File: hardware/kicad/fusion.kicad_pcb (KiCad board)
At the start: 2 copper layers, 33 x 59.9 mm, 36 parts, among them J1 BATTERY, J2 LSM6DSOX, J3 PICKIT, J4 HC-05, J5 FLEX, J7 FTDI, SW1 BUTTON, SW2 POWER, SW3 UART, U1 MCP1603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

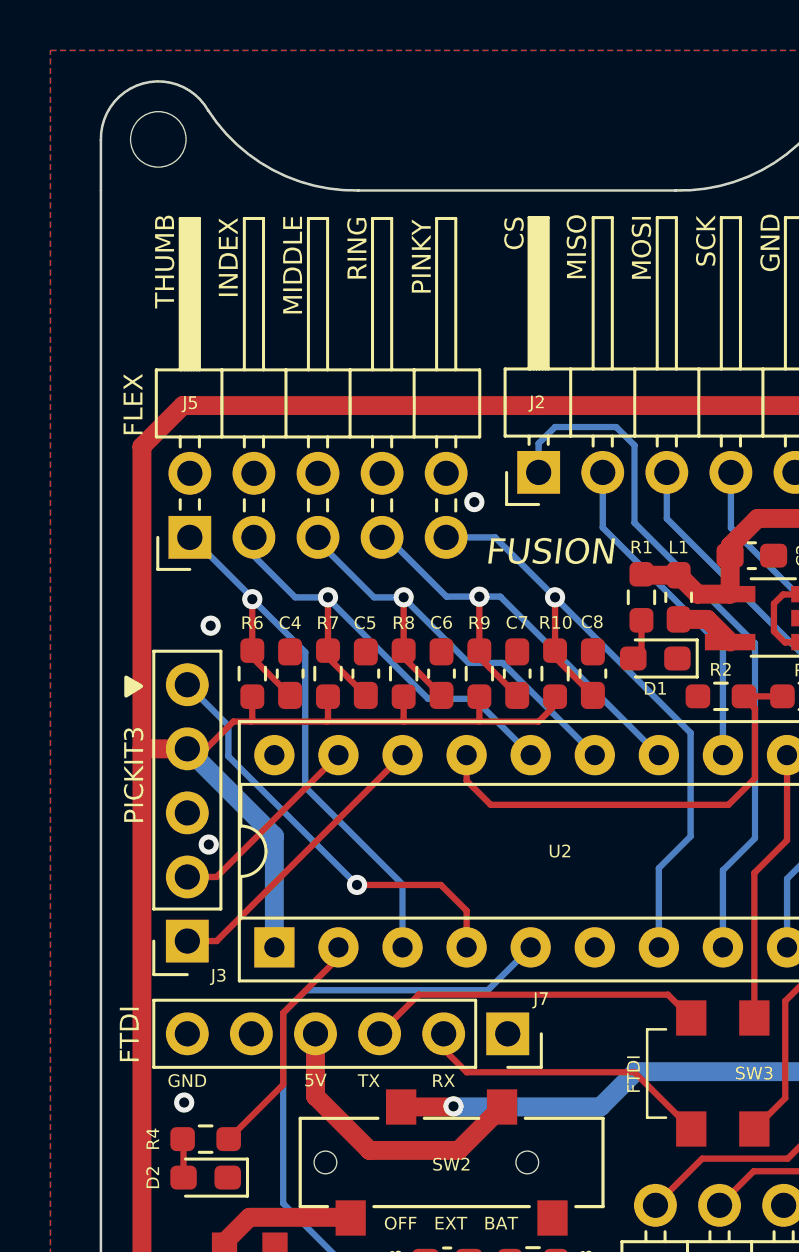
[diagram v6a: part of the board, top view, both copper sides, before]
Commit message: Rename FTDI to USB
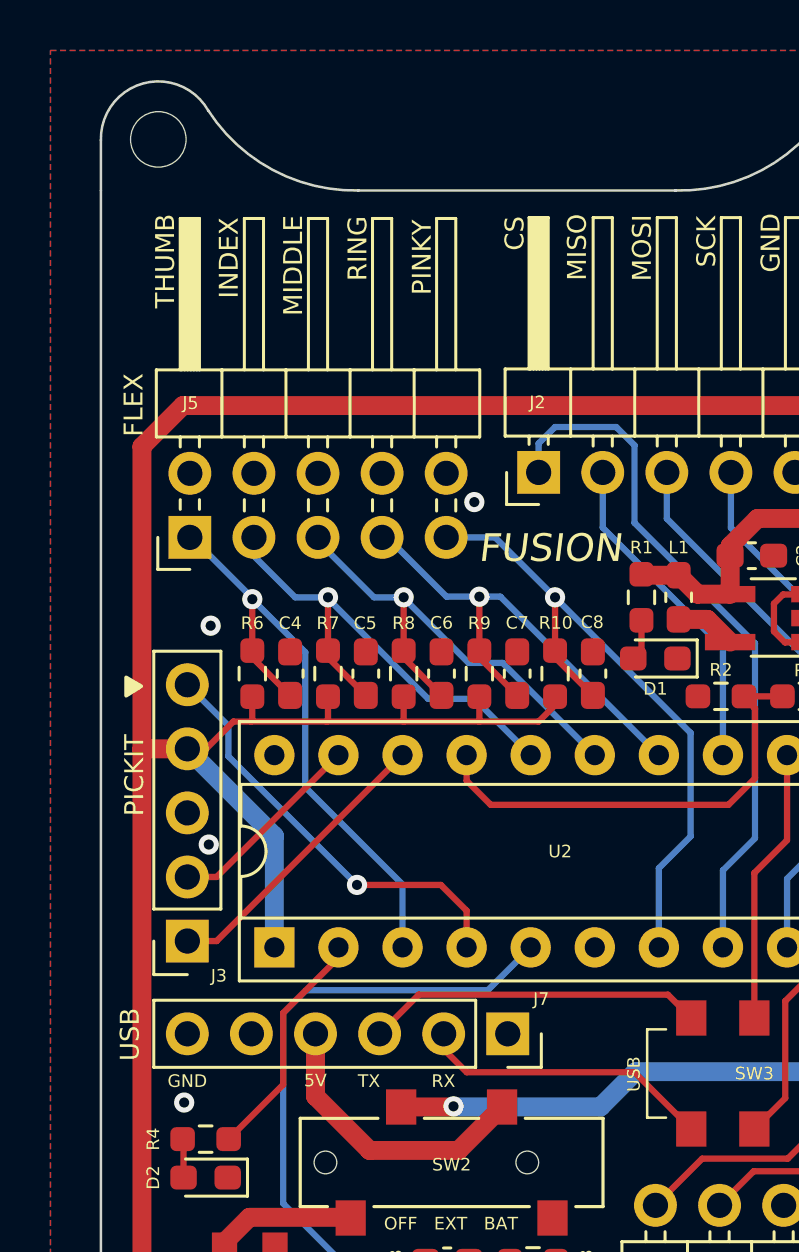
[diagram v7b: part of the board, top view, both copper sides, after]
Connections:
- net FTDI_5V renamed USB_5V
- net FTDI_RX renamed USB_RX
- net FTDI_TX renamed USB_TX
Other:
- board text added: "PICKIT"
- board text added: "USB"
- board text removed: "FTDI"
- board text removed: "PICKIT3"
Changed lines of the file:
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@@
   (net 16 "THUMB")
   (net 17 "unconnected-(J7-Pad1)")
-  (net 18 "FTDI_RX")
-  (net 19 "FTDI_TX")
-  (net 20 "FTDI_5V")
+  (net 18 "USB_RX")
+  (net 19 "USB_TX")
+  (net 20 "USB_5V")
   (net 21 "unconnected-(J7-Pad5)")
   (net 22 "Net-(D1-Pad2)")
@@
       (net 17 "unconnected-(J7-Pad1)") (pinfunction "Pin_1") (pintype "passive+no_connect"))
     (pad "2" thru_hole oval (at 0 2.54 270) (size 1.7 1.7) (drill 1) (layers *.Cu *.Mask)
-      (net 18 "FTDI_RX") (pinfunction "Pin_2") (pintype "passive"))
+      (net 18 "USB_RX") (pinfunction "Pin_2") (pintype "passive"))
     (pad "3" thru_hole oval (at 0 5.08 270) (size 1.7 1.7) (drill 1) (layers *.Cu *.Mask)
-      (net 19 "FTDI_TX") (pinfunction "Pin_3") (pintype "passive"))
+      (net 19 "USB_TX") (pinfunction "Pin_3") (pintype "passive"))
     (pad "4" thru_hole oval (at 0 7.62 270) (size 1.7 1.7) (drill 1) (layers *.Cu *.Mask)
-      (net 20 "FTDI_5V") (pinfunction "Pin_4") (pintype "passive"))
+      (net 20 "USB_5V") (pinfunction "Pin_4") (pintype "passive"))
     (pad "5" thru_hole oval (at 0 10.16 270) (size 1.7 1.7) (drill 1) (layers *.Cu *.Mask)
       (net 21 "unconnected-(J7-Pad5)") (pinfunction "Pin_5") (pintype "passive+no_connect"))
@@
       (net 23 "BUTTON") (pinfunction "RC5/CCP1/P1A") (pintype "bidirectional"))
     (pad "6" thru_hole oval (at 0 12.7 90) (size 1.6 1.6) (drill 0.8) (layers *.Cu *.Mask)
-      (net 33 "unconnected-(U2-Pad6)") (pinfunction "RC4/C2OUT/P1B") (pintype "bidirectional"))
+      (net 33 "unconnected-(U2-Pad6)") (pinfunction "RC4/C2OUT/P1B") (pintype "bidirectional+no_connect"))
     (pad "7" thru_hole oval (at 0 15.24 90) (size 1.6 1.6) (drill 0.8) (layers *.Cu *.Mask)
       (net 12 "PINKY") (pinfunction "RC3/AN7/C12IN3-/P1C") (pintype "bidirectional"))
@@
       (net 24 "RX") (pinfunction "B") (pintype "passive"))
     (pad "3" smd rect (at 2.5 2.2 180) (size 1.2 1.4) (layers "F.Cu" "F.Paste" "F.Mask")
-      (net 19 "FTDI_TX") (pinfunction "C") (pintype "passive"))
+      (net 19 "USB_TX") (pinfunction "C") (pintype "passive"))
     (pad "4" smd rect (at -2.5 -2.2 180) (size 1.2 1.4) (layers "F.Cu" "F.Paste" "F.Mask")
       (net 11 "BT_RX") (pinfunction "A") (pintype "passive"))
@@
       (net 25 "TX") (pinfunction "B") (pintype "passive"))
     (pad "6" smd rect (at 2.5 -2.2 180) (size 1.2 1.4) (layers "F.Cu" "F.Paste" "F.Mask")
-      (net 18 "FTDI_RX") (pinfunction "C") (pintype "passive"))
+      (net 18 "USB_RX") (pinfunction "C") (pintype "passive"))
     (model "${KIPRJMOD}/models/SPDT.step"
       (offset (xyz 0 0 3.5))
@@
       (net 31 "unconnected-(SW2-Pad1)") (pinfunction "1") (pintype "passive+no_connect"))
     (pad "2" smd rect (at -2 2.2 180) (size 1.2 1.4) (layers "F.Cu" "F.Paste" "F.Mask")
-      (net 20 "FTDI_5V") (pinfunction "2") (pintype "passive"))
+      (net 20 "USB_5V") (pinfunction "2") (pintype "passive"))
     (pad "3" smd rect (at 2 2.2 180) (size 1.2 1.4) (layers "F.Cu" "F.Paste" "F.Mask")
       (net 26 "Net-(C1-Pad1)") (pinfunction "3") (pintype "passive"))
@@
   (gr_arc (start 165.775 64.825) (mid 163.190649 67.197979) (end 159.775 68) (layer "Edge.Cuts") (width 0.1))
   (gr_arc (start 159.824452 119.3) (mid 163.212162 120.114076) (end 165.774452 122.475) (layer "Edge.Cuts") (width 0.1))
-  (gr_arc (start 137 66) (mid 138.667917 63.758017) (end 141.250548 64.825) (layer "Edge.Cuts") (width 0.1))
+  (gr_arc (start 137 66) (mid 138.667917 63.758018) (end 141.250548 64.825) (layer "Edge.Cuts") (width 0.1))
   (gr_arc (start 165.775 64.825) (mid 168.357369 63.758186) (end 170.025 66) (layer "Edge.Cuts") (width 0.1))
   (gr_line (start 137 119.3) (end 137 68) (layer "Edge.Cuts") (width 0.1))
@@
     (effects (font (size 0.5 0.5) (thickness 0.1)))
   )
-  (gr_text "FUSION" (at 154.8 82.325) (layer "F.SilkS")
-    (effects (font (size 1 1) (thickness 0.25) italic))
+  (gr_text "FUSION" (at 154.8 82.175) (layer "F.SilkS")
+    (effects (font (size 1.1 1.1) (thickness 0.275) italic))
   )
   (gr_text "TX" (at 160.525 117.75 90) (layer "F.SilkS")
@@
     (effects (font (size 0.75 0.75) (thickness 0.125)))
   )
-  (gr_text "FTDI" (at 158.125 103.025 90) (layer "F.SilkS")
+  (gr_text "USB" (at 158.125 103.025 90) (layer "F.SilkS")
     (effects (font (size 0.5 0.5) (thickness 0.1)))
   )
-  (gr_text "PICKIT3" (at 138.325 91.175 90) (layer "F.SilkS")
+  (gr_text "PICKIT" (at 138.325 91.175 90) (layer "F.SilkS")
     (effects (font (size 0.75 0.75) (thickness 0.125)))
   )
@@
     (effects (font (size 0.75 0.75) (thickness 0.125)))
   )
-  (gr_text "FTDI" (at 138.15 101.45 90) (layer "F.SilkS")
-    (effects (font (size 0.75 0.75) (thickness 0.125)))
-  )
+  (gr_text "USB" (at 138.15 101.45 90) (layer "F.SilkS")
+    (effects (font (size 0.75 0.75) (thickness 0.125)))
+  )

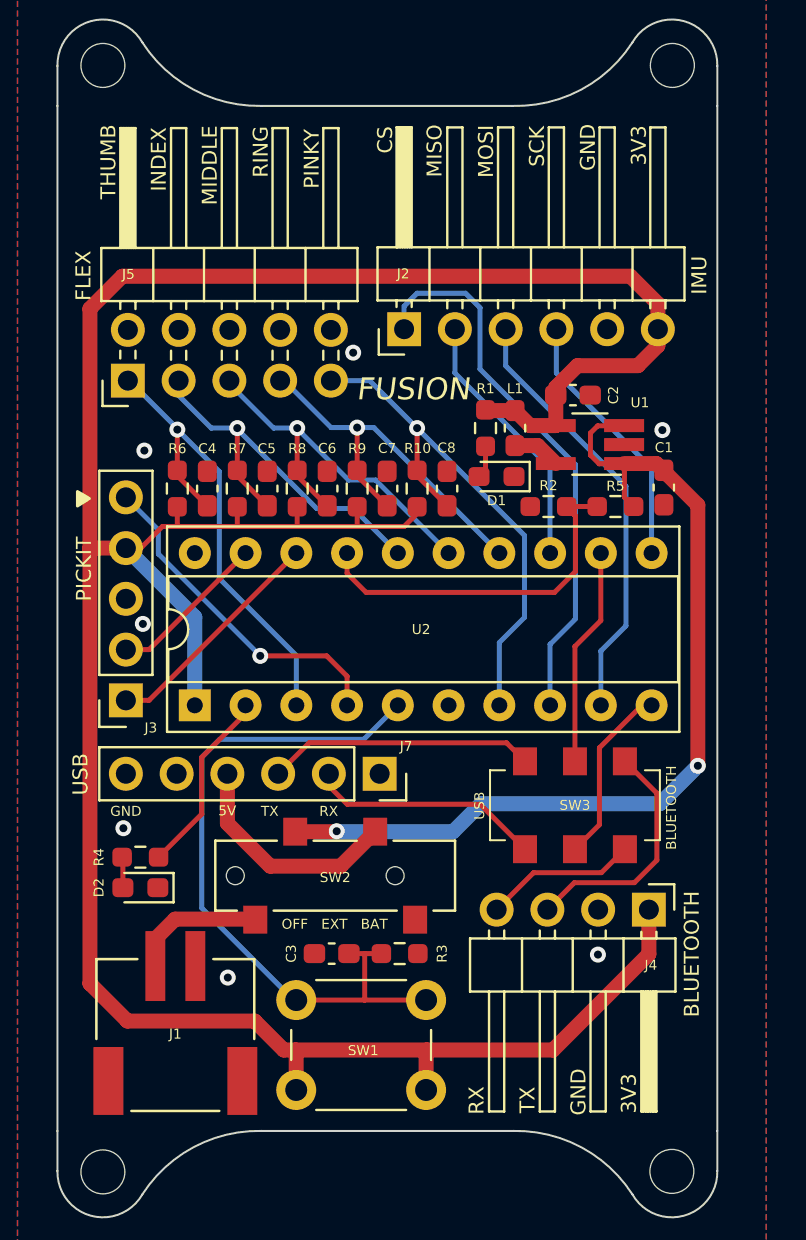
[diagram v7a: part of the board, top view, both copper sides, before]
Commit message: Power HC-05 from raw power source
BT module has an LDO that requires at least 3V6.
Powering from 3V3 causes improper regulation and
browns out the entire system.
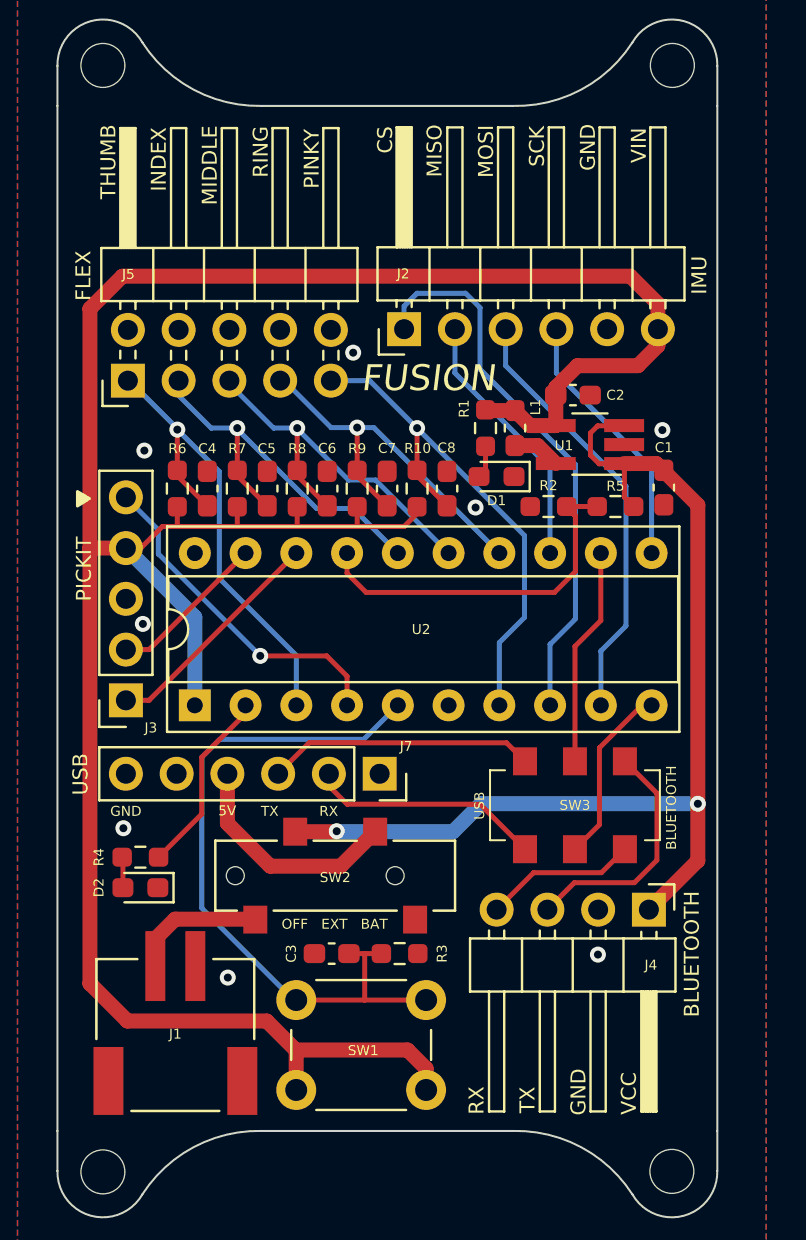
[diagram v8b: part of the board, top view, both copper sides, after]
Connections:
- C1 pad 1: Net-(C1-Pad1) -> VDC
- J4 pad 1: +3V3 -> VDC
- R5 pad 1: Net-(C1-Pad1) -> VDC
- SW2 pad 3: Net-(C1-Pad1) -> VDC
- U1 pad 1: Net-(C1-Pad1) -> VDC
- U1 pad 3: Net-(C1-Pad1) -> VDC
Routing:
- net VDC: track 0.00 -> 53.7 mm, vias 0 -> 2
- net Net-(C1-Pad1): track 46.3 -> 0.00 mm, vias 2 -> 0
- net +3V3: track 145.6 -> 129.7 mm
- net GNDREF: vias 7 -> 8
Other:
- board text added: "VCC"
- board text added: "VIN"
- board text removed: "3V3"
